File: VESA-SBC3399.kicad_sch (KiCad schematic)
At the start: 0 parts

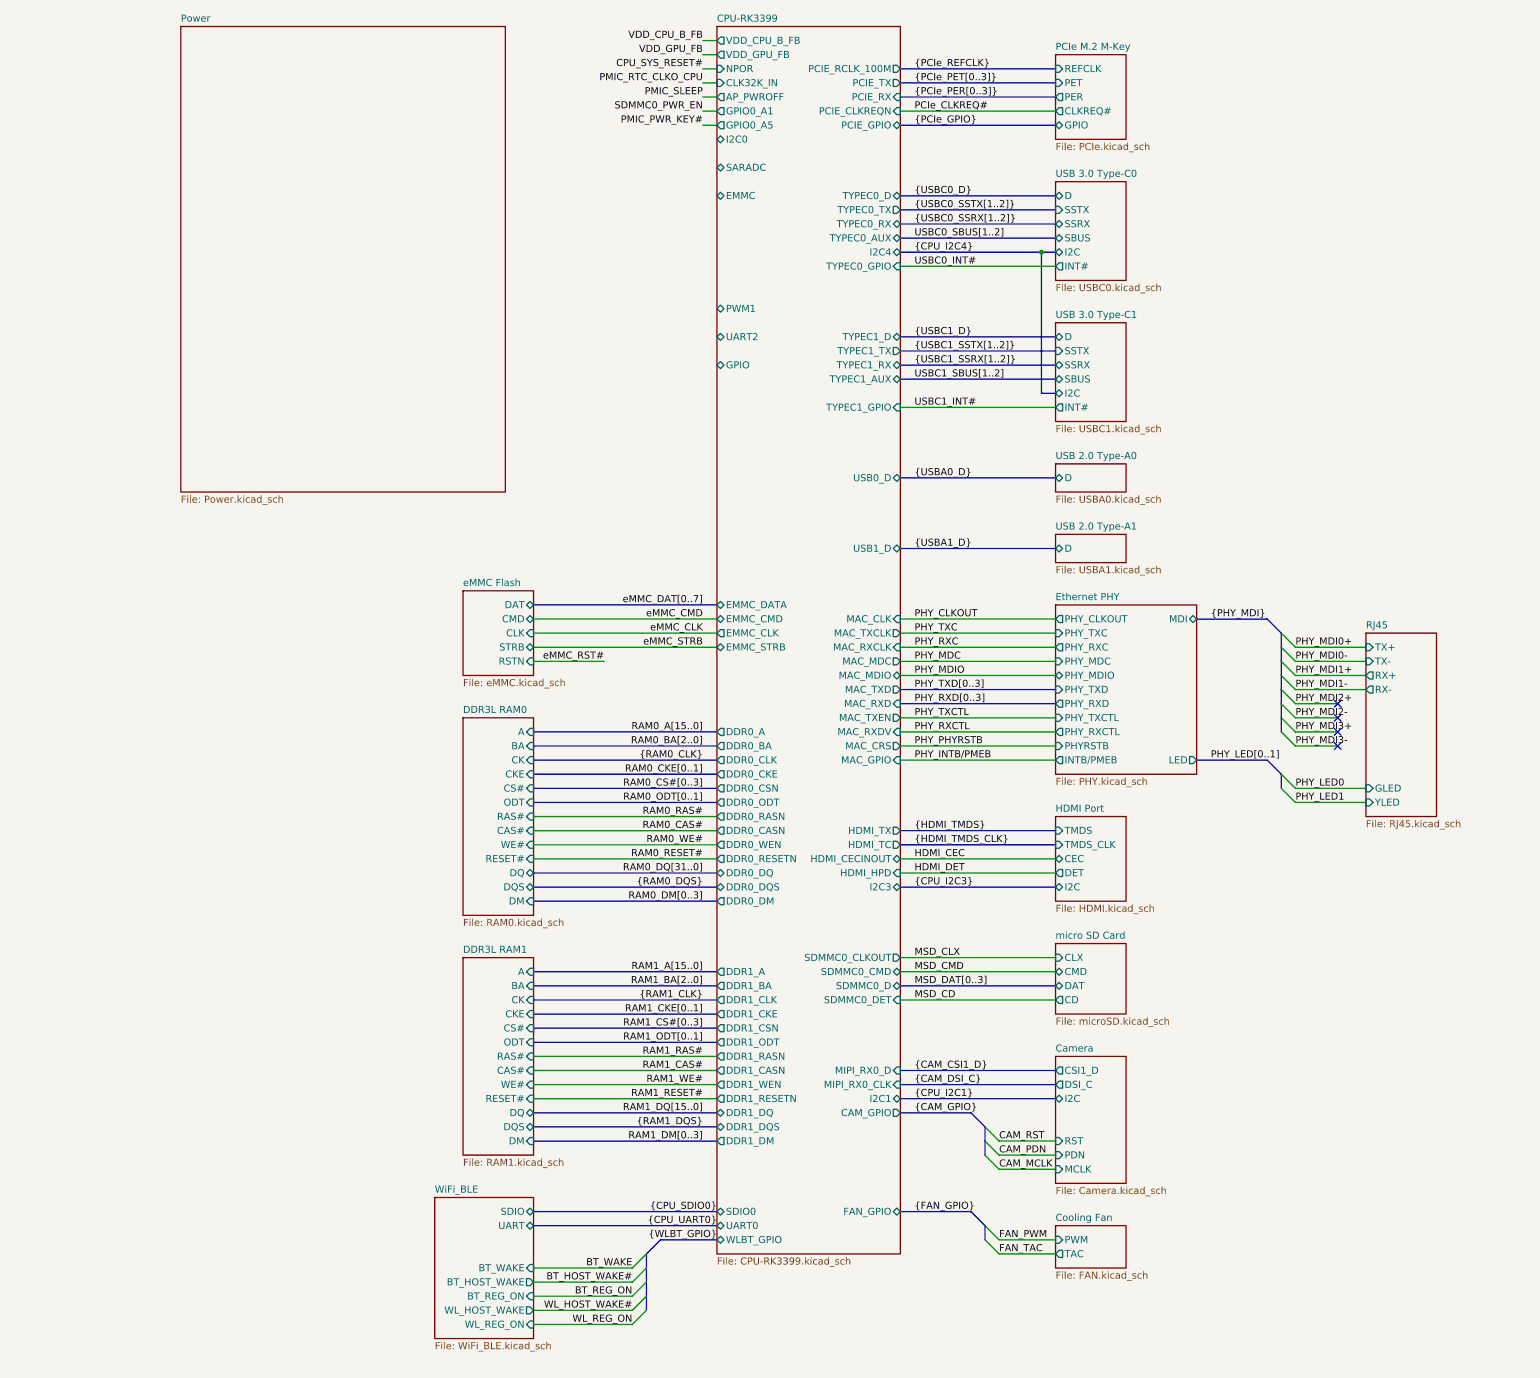
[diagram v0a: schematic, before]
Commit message: update schematic
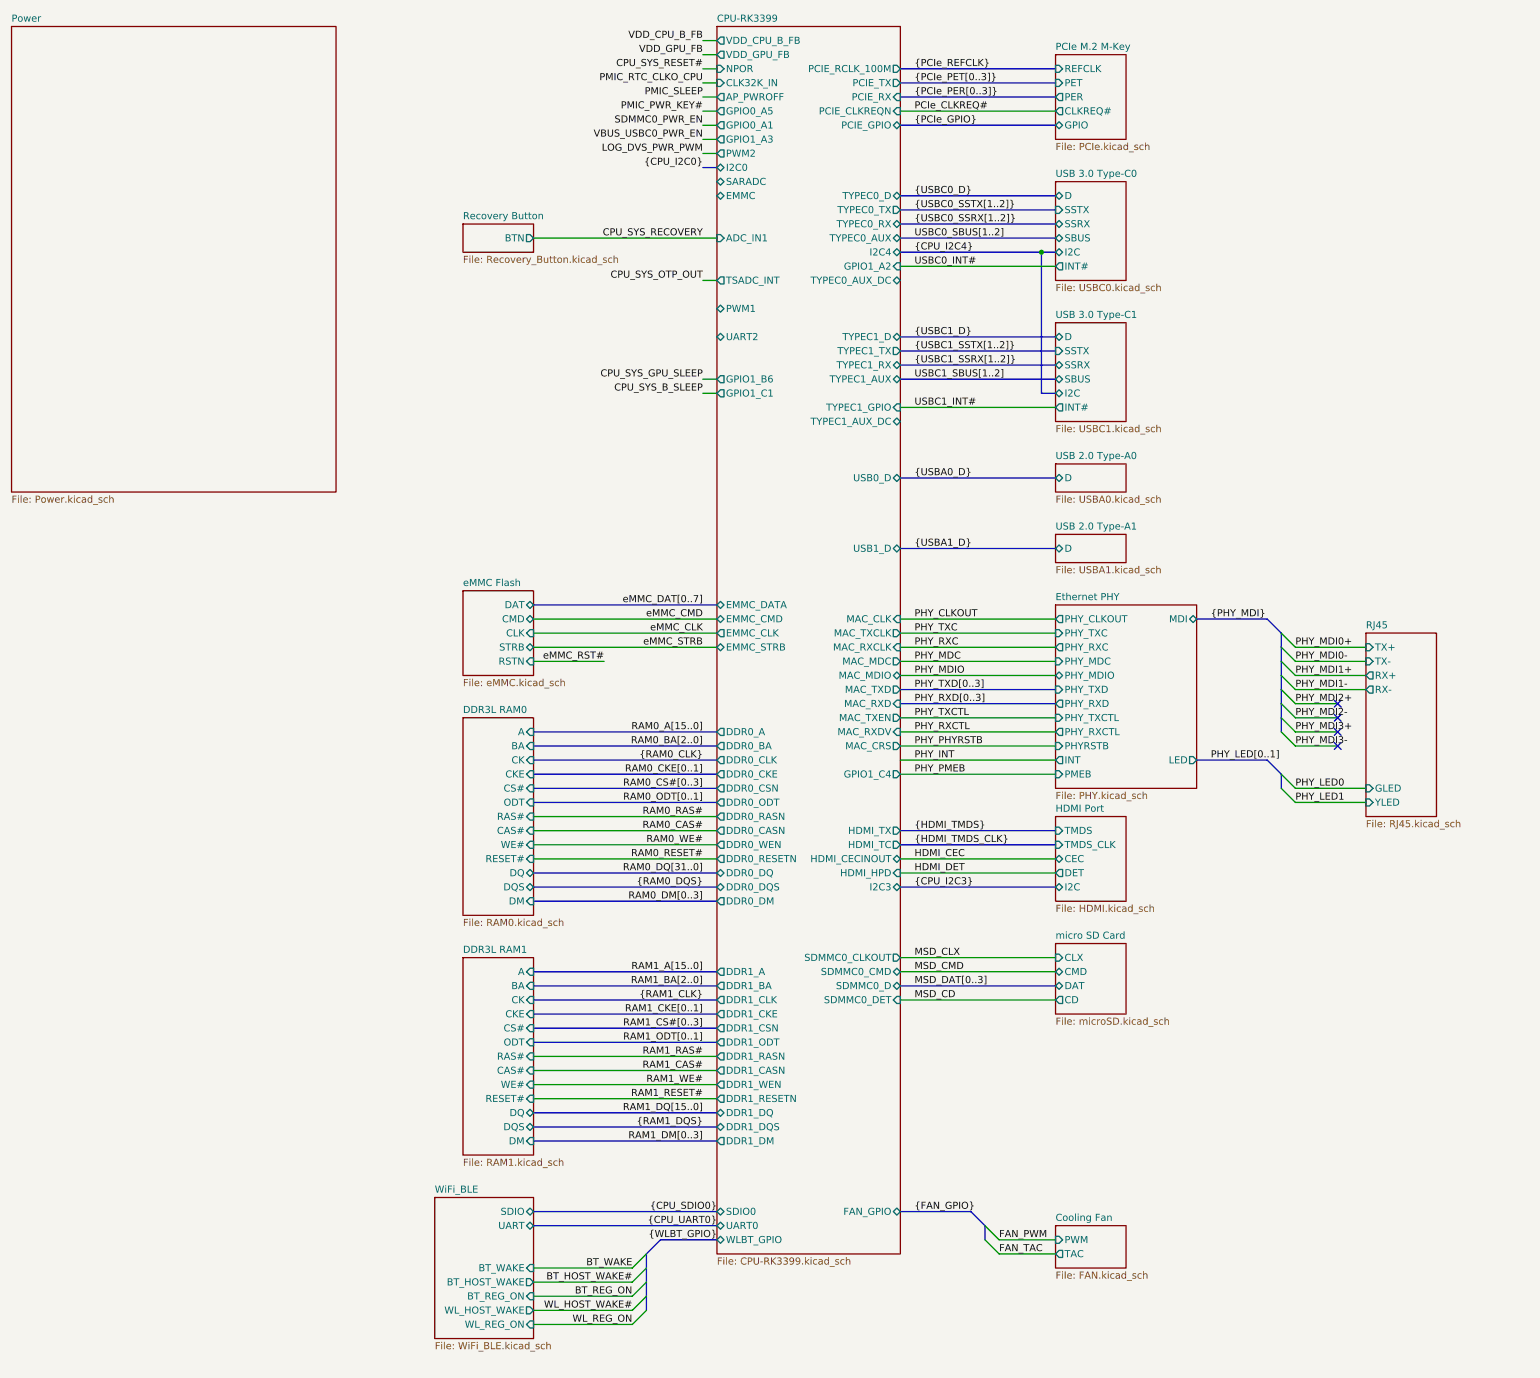
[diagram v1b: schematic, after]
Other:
- removed sheet Camera
- added sheet Recovery Button (Recovery_Button.kicad_sch)
- sheet CPU-RK3399 ports: added ADC_IN1, GPIO1_A2, GPIO1_A3, GPIO1_B6, GPIO1_C1, GPIO1_C4, PWM2, TSADC_INT, TYPEC0_AUX_DC, TYPEC1_AUX_DC; removed CAM_GPIO, GPIO, I2C1, MAC_GPIO, MIPI_RX0_CLK, MIPI_RX0_D, TYPEC0_GPIO
- sheet Ethernet PHY ports: added INT, PMEB; removed INTB/PMEB

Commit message: design PMIC
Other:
- sheet CPU-RK3399 ports: added GPIO1_C5, GPIO1_C7, GPIO1_D0; removed none
- sheet Power ports: added I2C0, PMIC_CLK32KOUT1, PMIC_CLK32KOUT2, PMIC_INT, PMIC_NRESPWRON, PMIC_OTP, PMIC_PWRON, PMIC_SLEEP; removed none
- sheet WiFi_BLE ports: added LPO; removed none

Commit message: update design power
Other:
- sheet CPU-RK3399 ports: added none; removed EMMC, SARADC
- sheet Power ports: added 0V9_VDD_CPU_B_FB, 0V9_VDD_CPU_B_VSEL, 0V9_VDD_GPU_FB; removed none

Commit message: finish design power
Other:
- sheet Power ports: added 0V9_VDD_GPU_VSEL, 0V9_VDD_LOG_DVS_PWR_PWM, 3V3_VCC_SD_EN; removed none
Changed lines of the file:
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@@
 		)
 	)
-	(wire
-		(pts
-			(xy 172.72 68.58) (xy 175.26 68.58)
-		)
-		(stroke
-			(width 0)
-			(type default)
-		)
-	)
 	(bus
 		(pts
@@
 		)
 	)
-	(wire
-		(pts
-			(xy 172.72 104.14) (xy 175.26 104.14)
-		)
-		(stroke
-			(width 0)
-			(type default)
-		)
-	)
 	(bus
 		(pts
@@
 		)
 	)
-	(wire
-		(pts
-			(xy 172.72 109.22) (xy 175.26 109.22)
-		)
-		(stroke
-			(width 0)
-			(type default)
-		)
-	)
 	(bus
 		(pts
@@
 	(wire
 		(pts
-			(xy 142.24 76.2) (xy 175.26 76.2)
+			(xy 111.76 73.66) (xy 175.26 73.66)
+		)
+		(stroke
+			(width 0)
+			(type default)
+		)
+	)
+	(wire
+		(pts
+			(xy 142.24 91.44) (xy 175.26 91.44)
 		)
 		(stroke
@@
 		)
 	)
+	(wire
+		(pts
+			(xy 111.76 68.58) (xy 175.26 68.58)
+		)
+		(stroke
+			(width 0)
+			(type default)
+		)
+	)
 	(bus
 		(pts
@@
 	(wire
 		(pts
-			(xy 172.72 73.66) (xy 175.26 73.66)
+			(xy 172.72 88.9) (xy 175.26 88.9)
 		)
 		(stroke
@@
 	(wire
 		(pts
+			(xy 111.76 78.74) (xy 175.26 78.74)
+		)
+		(stroke
+			(width 0)
+			(type default)
+		)
+	)
+	(wire
+		(pts
 			(xy 142.24 139.7) (xy 175.26 139.7)
 		)
@@
 	)
 	(label "LOG_DVS_PWR_PWM"
-		(at 172.72 109.22 180)
+		(at 172.72 78.74 180)
 		(effects
 			(font
@@
 	)
 	(label "SDMMC0_PWR_EN"
-		(at 172.72 104.14 180)
+		(at 172.72 73.66 180)
 		(effects
 			(font
@@
 	)
 	(label "PCIe_PWR_EN"
-		(at 172.72 73.66 180)
+		(at 172.72 88.9 180)
 		(effects
 			(font
@@
 	)
 	(label "CPU_SYS_RECOVERY"
-		(at 172.72 76.2 180)
+		(at 172.72 91.44 180)
 		(effects
 			(font
@@
 	)
 	(sheet
-		(at 129.54 73.66)
+		(at 129.54 88.9)
 		(size 12.7 5.08)
 		(exclude_from_sim no)
@@
 		)
 		(property "Sheetname" "Recovery Button"
-			(at 129.54 72.9484 0)
+			(at 129.54 88.1884 0)
 			(effects
 				(font
@@
 		)
 		(property "Sheetfile" "Recovery_Button.kicad_sch"
-			(at 129.54 79.3246 0)
+			(at 129.54 94.5646 0)
 			(effects
 				(font
@@
 		)
 		(pin "BTN" output
-			(at 142.24 76.2 0)
+			(at 142.24 91.44 0)
 			(effects
 				(font
@@
 		)
 		(pin "PWM1" bidirectional
-			(at 175.26 78.74 180)
+			(at 175.26 93.98 180)
 			(effects
 				(font
@@
 		)
 		(pin "UART2" bidirectional
-			(at 175.26 83.82 180)
+			(at 175.26 99.06 180)
 			(effects
 				(font
@@
 		)
 		(pin "GPIO0_A1" output
-			(at 175.26 104.14 180)
+			(at 175.26 73.66 180)
 			(effects
 				(font
@@
 		)
 		(pin "ADC_IN1" input
-			(at 175.26 76.2 180)
+			(at 175.26 91.44 180)
 			(effects
 				(font
@@
 		)
 		(pin "PWM2" output
-			(at 175.26 109.22 180)
+			(at 175.26 78.74 180)
 			(effects
 				(font
@@
 		)
 		(pin "GPIO1_D0" output
-			(at 175.26 73.66 180)
+			(at 175.26 88.9 180)
 			(effects
 				(font
@@
 			(effects
 				(font
+					(size 1.27 1.27)
+				)
+				(justify right)
+			)
+		)
+		(pin "0V9_VDD_GPU_VSEL" input
+			(at 111.76 68.58 0)
+			(effects
+				(font
+					(size 1.27 1.27)
+				)
+				(justify right)
+			)
+		)
+		(pin "3V3_VCC_SD_EN" input
+			(at 111.76 73.66 0)
+			(effects
+				(font
+					(size 1.27 1.27)
+				)
+				(justify right)
+			)
+		)
+		(pin "0V9_VDD_LOG_DVS_PWR_PWM" input
+			(at 111.76 78.74 0)
+			(effects
+				(font

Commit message: design USB-A
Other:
- sheet USB 2.0 Type-A0 renamed USB 2.0 Type-A
- removed sheet USB 2.0 Type-A1
- sheet USB 2.0 Type-A: file USBA0.kicad_sch -> USBA.kicad_sch
- sheet USB 2.0 Type-A ports: added USB_D0, USB_D1; removed D
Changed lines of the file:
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@@
 	(bus
 		(pts
-			(xy 208.28 121.92) (xy 236.22 121.92)
+			(xy 208.28 111.76) (xy 236.22 111.76)
 		)
 		(stroke
@@
 	)
 	(label "{USBA1_D}"
-		(at 210.82 121.92 0)
+		(at 210.82 111.76 0)
 		(effects
 			(font
@@
 	)
 	(sheet
-		(at 236.22 119.38)
-		(size 12.7 5.08)
+		(at 236.22 106.68)
+		(size 12.7 7.62)
 		(exclude_from_sim no)
 		(in_bom yes)
@@
 			(color 0 255 255 0.1000)
 		)
-		(property "Sheetname" "USB 2.0 Type-A1"
-			(at 236.22 118.6684 0)
+		(property "Sheetname" "USB 2.0 Type-A"
+			(at 236.22 105.9684 0)
 			(effects
 				(font
@@
 			)
 		)
-		(property "Sheetfile" "USBA1.kicad_sch"
-			(at 236.22 125.0446 0)
+		(property "Sheetfile" "USBA.kicad_sch"
+			(at 236.22 114.8846 0)
 			(effects
 				(font
@@
 			)
 		)
-		(pin "D" bidirectional
-			(at 236.22 121.92 180)
+		(pin "USB_D0" bidirectional
+			(at 236.22 109.22 180)
 			(effects
 				(font
@@
 			)
 		)
-		(instances
-			(project "VESA-SBC3399"
-				(path "/ebc9dc57-8b05-484a-a5cd-c53b1efc71d3"
-					(page "7")
-				)
-			)
-		)
-	)
-	(sheet
-		(at 236.22 106.68)
-		(size 12.7 5.08)
-		(exclude_from_sim no)
-		(in_bom yes)
-		(on_board yes)
-		(dnp no)
-		(fields_autoplaced yes)
-		(stroke
-			(width 0.1524)
-			(type solid)
-		)
-		(fill
-			(color 0 255 255 0.1000)
-		)
-		(property "Sheetname" "USB 2.0 Type-A0"
-			(at 236.22 105.9684 0)
-			(effects
-				(font
-					(size 1.27 1.27)
-				)
-				(justify left bottom)
-			)
-		)
-		(property "Sheetfile" "USBA0.kicad_sch"
-			(at 236.22 112.3446 0)
-			(effects
-				(font
-					(size 1.27 1.27)
-				)
-				(justify left top)
-			)
-		)
-		(pin "D" bidirectional
-			(at 236.22 109.22 180)
+		(pin "USB_D1" bidirectional
+			(at 236.22 111.76 180)
 			(effects
 				(font
@@
 		)
 		(pin "USB1_D" bidirectional
-			(at 208.28 121.92 0)
+			(at 208.28 111.76 0)
 			(effects
 				(font
@@
 	)
 	(sheet
-		(at 53.34 33.02)
-		(size 58.42 78.74)
+		(at 78.74 33.02)
+		(size 33.02 48.26)
 		(exclude_from_sim no)
 		(in_bom yes)
@@
 		)
 		(property "Sheetname" "Power"
-			(at 53.34 32.3084 0)
+			(at 78.74 32.3084 0)
 			(effects
 				(font
@@
 		)
 		(property "Sheetfile" "Power.kicad_sch"
-			(at 53.34 112.3446 0)
+			(at 78.74 81.8646 0)
 			(effects
 				(font

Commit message: design DDR
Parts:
- added MEC1, MEC2, MEC3, MEC4: ~, footprints:M4_Hole, symbol component_library:Mechanical/M4_Hole
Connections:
- new net CHGND: MEC1.1, MEC2.1, MEC3.1, MEC4.1
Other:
- sheet CPU-RK3399 ports: added GPIO1_A1, GPIO4_D2, TYPEC0_U2VBUSDET, TYPEC1_U2VBUSDET; removed TYPEC1_GPIO
- sheet USB 2.0 Type-A ports: added VBUS_USBA_EN; removed none
- sheet USB 3.0 Type-C0 ports: added DC_SBUS, VBUS_USBC0_VBUSDET, VBUS_USBC_EN; removed none
- sheet USB 3.0 Type-C1 ports: added DC_SBUS, VBUS_USBC1_VBUSDET, VBUS_USBC_EN; removed none
